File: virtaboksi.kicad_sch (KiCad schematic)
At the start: 22 parts, among them J1 Conn_01x02_Female, J2 Conn_01x03_Female, J3 Conn_01x02_Female, J4 Conn_01x02_Female, J5 Conn_01x02_Female, J6 Conn_01x02_Female, J7 Conn_01x02_Female, Q1 IRF9540N, Q2 IRF9540N, Q3 IRF9540N

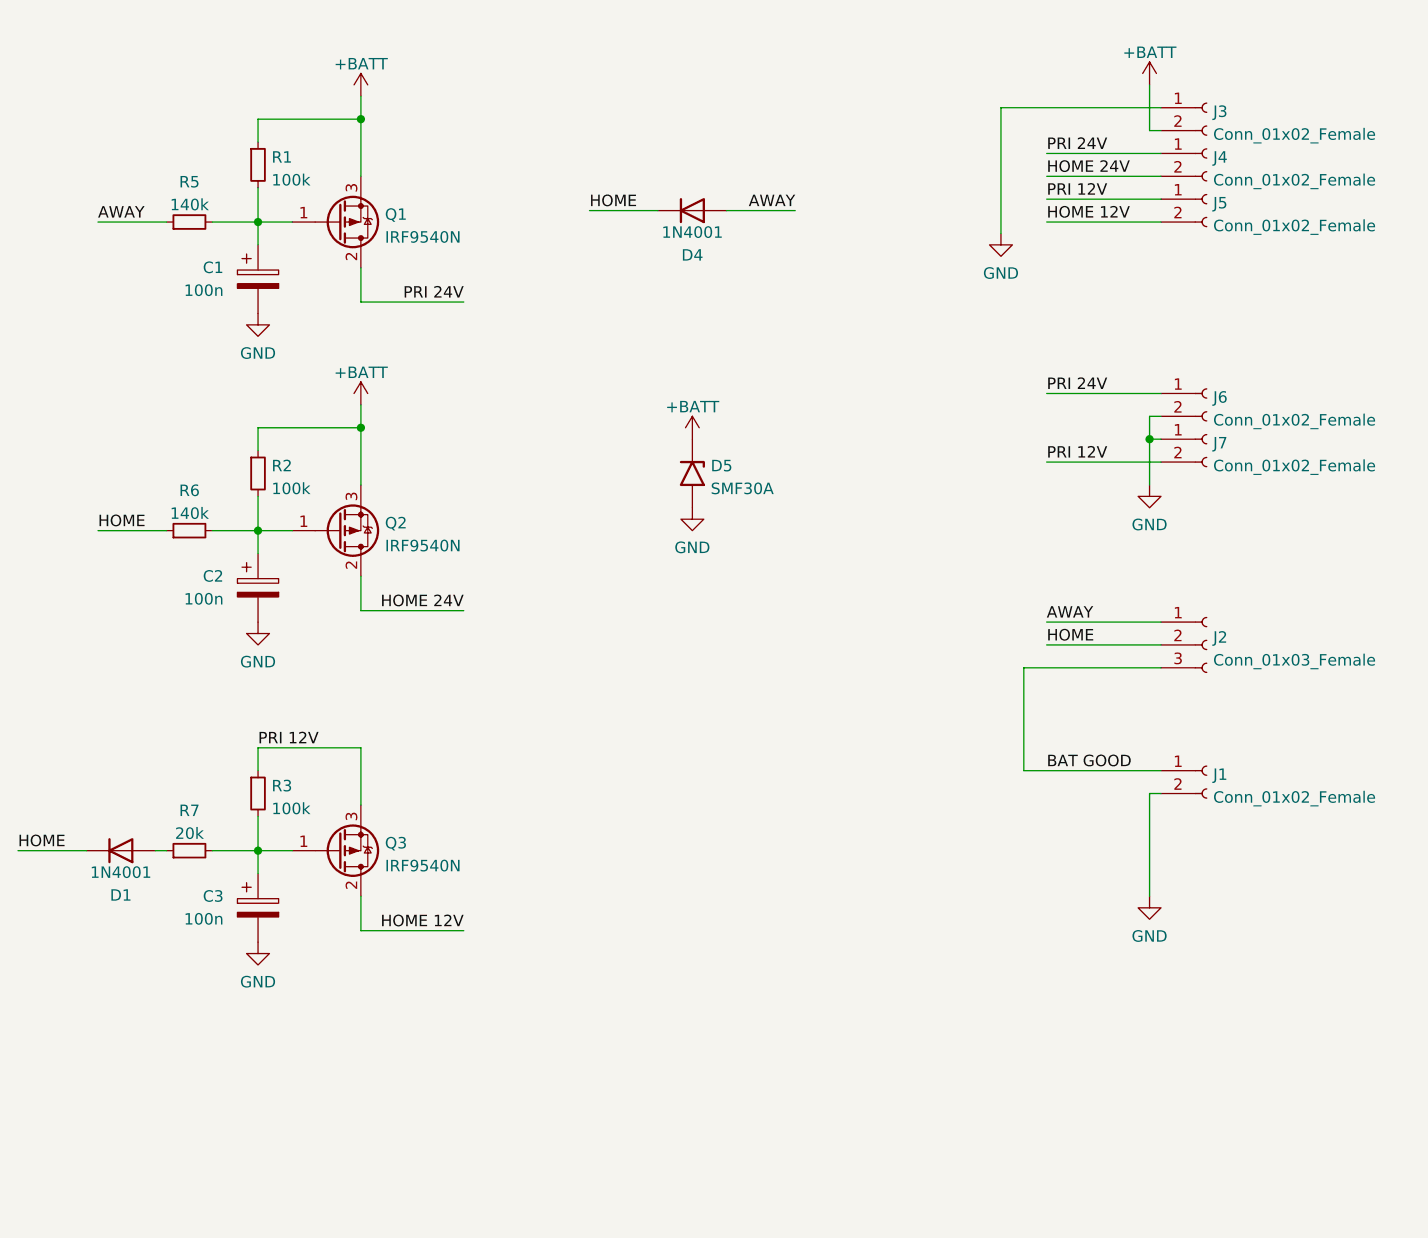
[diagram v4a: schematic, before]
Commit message: Change caps from elco to ceramic, reannotate
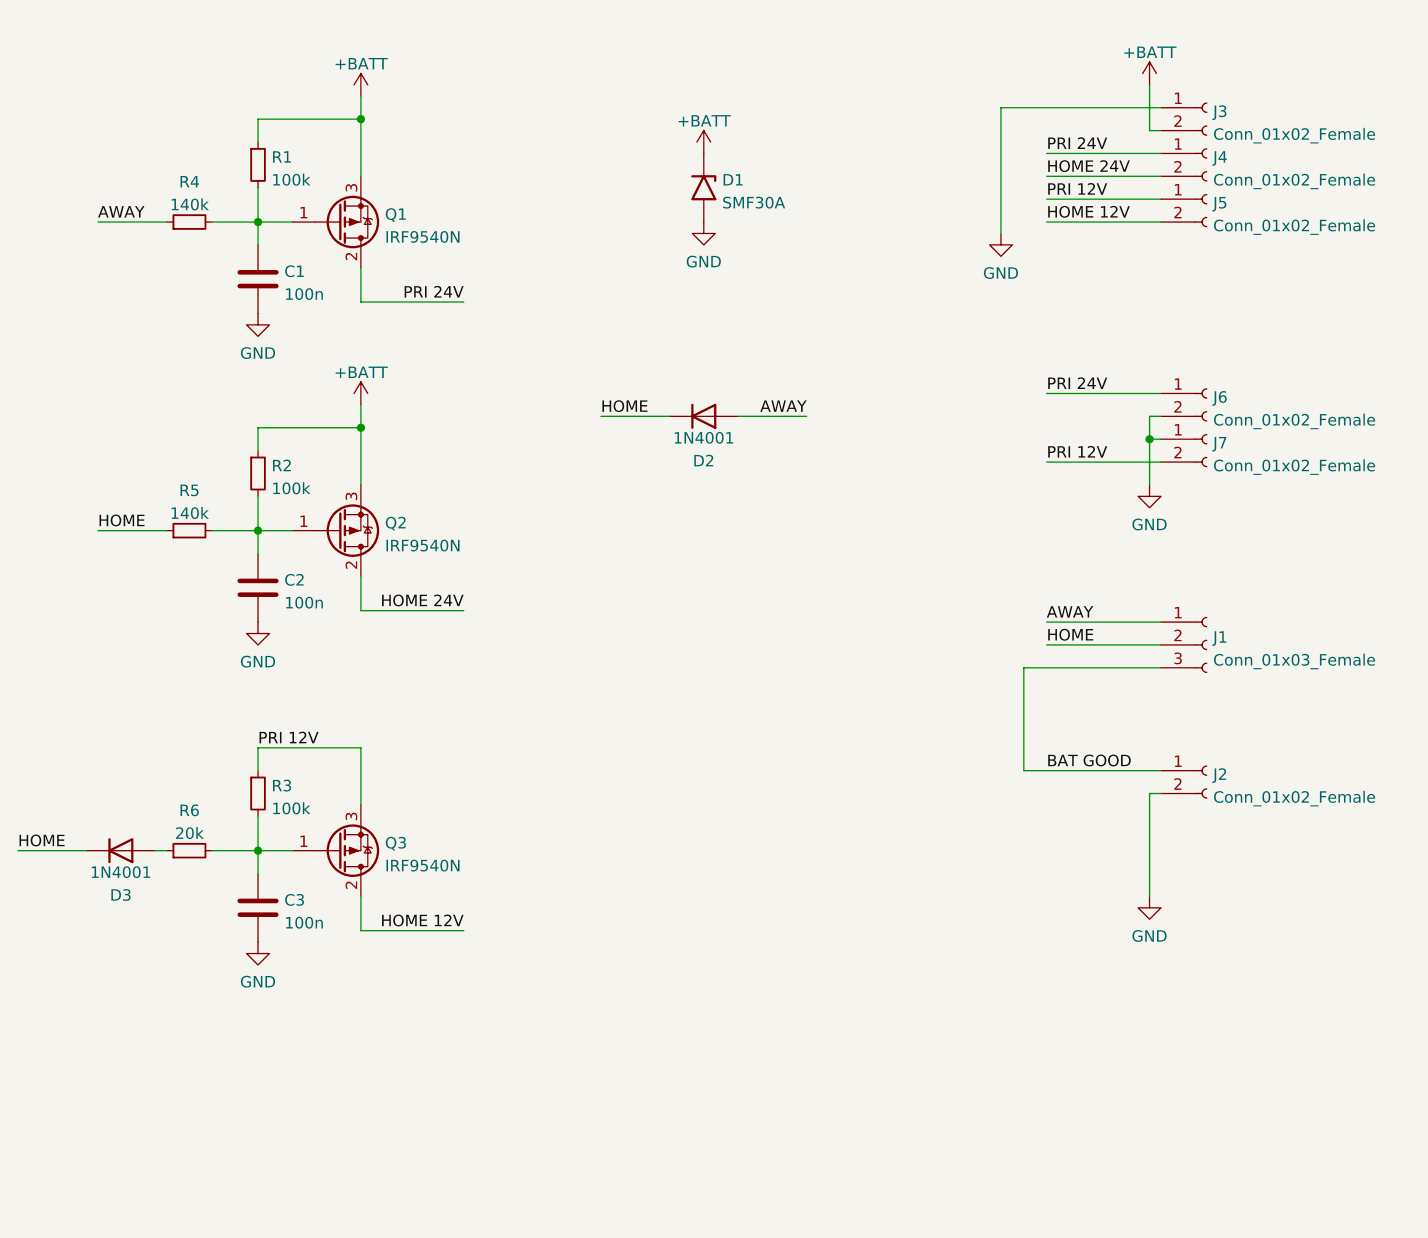
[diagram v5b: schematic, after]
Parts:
- removed C1, C2, C3: 100n, Capacitor_THT:CP_Radial_D6.3mm_P2.50mm, symbol Device:C_Polarized
- added C1, C2, C3: 100n, Capacitor_THT:C_Disc_D4.7mm_W2.5mm_P5.00mm, symbol Device:C
- renumbered D5 to D1, D4 to D2, D1 to D3, J2 to J1, J1 to J2, R5 to R4, R6 to R5, R7 to R6
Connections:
- net GND: now also C1.2, C2.2, C3.2
- net at Q1.1 (G), R1.2, R4.2: now also C1.1
- net at Q2.1 (G), R2.2, R5.2: now also C2.1
- net at Q3.1 (G), R3.2, R6.2: now also C3.1
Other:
- moved on the sheet: D1, D2

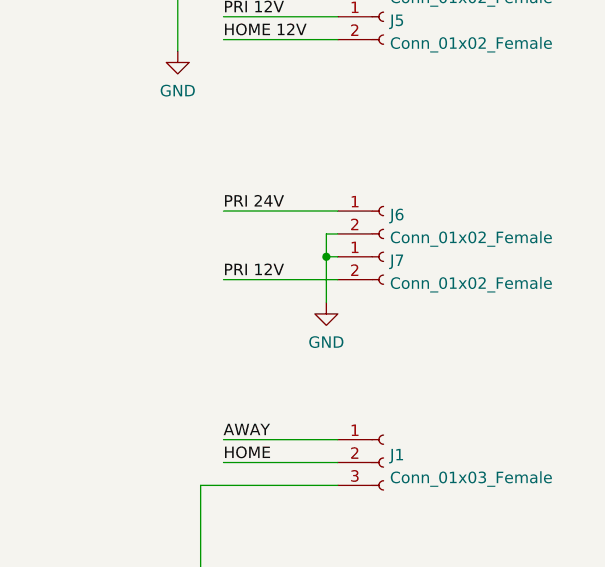
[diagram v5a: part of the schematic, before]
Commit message: Remove grounding pins for DC converter
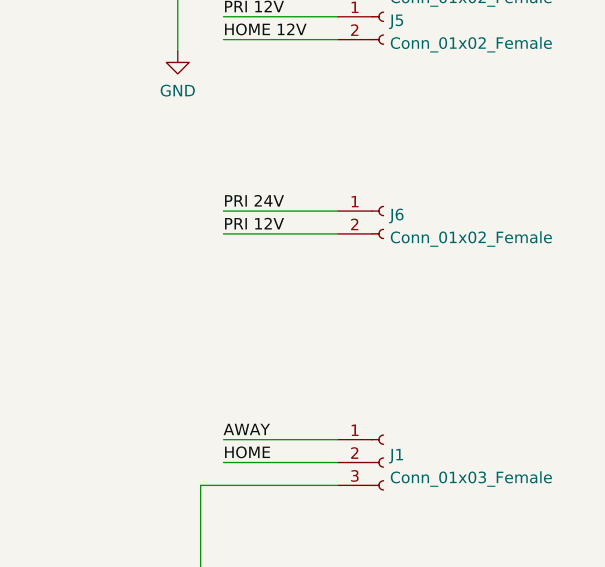
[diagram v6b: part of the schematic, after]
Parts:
- removed J7: Conn_01x02_Female, Powerpole:45A-VERT-PAIR, symbol Connector:Conn_01x02_Female
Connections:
- net GND: no longer J6.2 (Pin_2)
- net PRI 12V: now also J6.2 (Pin_2)
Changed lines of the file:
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@@
   (junction (at 76.2 72.39) (diameter 0) (color 0 0 0 0)
   )
-  (junction (at 163.83 73.66) (diameter 0) (color 0 0 0 0)
-  )
   (junction (at 76.2 38.1) (diameter 0) (color 0 0 0 0)
   )
@@
     (stroke (width 0) (type default) (color 0 0 0 0))
   )
-  (wire (pts (xy 163.83 73.66) (xy 165.1 73.66))
-    (stroke (width 0) (type default) (color 0 0 0 0))
-  )
   (wire (pts (xy 152.4 93.98) (xy 165.1 93.98))
     (stroke (width 0) (type default) (color 0 0 0 0))
@@
     (stroke (width 0) (type default) (color 0 0 0 0))
   )
-  (wire (pts (xy 163.83 71.12) (xy 163.83 73.66))
-    (stroke (width 0) (type default) (color 0 0 0 0))
-  )
   (wire (pts (xy 152.4 68.58) (xy 165.1 68.58))
     (stroke (width 0) (type default) (color 0 0 0 0))
@@
     (stroke (width 0) (type default) (color 0 0 0 0))
   )
-  (wire (pts (xy 163.83 71.12) (xy 165.1 71.12))
-    (stroke (width 0) (type default) (color 0 0 0 0))
-  )
   (wire (pts (xy 147.32 36.83) (xy 147.32 50.8))
     (stroke (width 0) (type default) (color 0 0 0 0))
@@
     (stroke (width 0) (type default) (color 0 0 0 0))
   )
-  (wire (pts (xy 152.4 76.2) (xy 165.1 76.2))
+  (wire (pts (xy 152.4 71.12) (xy 165.1 71.12))
     (stroke (width 0) (type default) (color 0 0 0 0))
   )
@@
   )
   (wire (pts (xy 87.63 92.71) (xy 76.2 92.71))
-    (stroke (width 0) (type default) (color 0 0 0 0))
-  )
-  (wire (pts (xy 163.83 73.66) (xy 163.83 78.74))
     (stroke (width 0) (type default) (color 0 0 0 0))
   )
@@
     (effects (font (size 1.27 1.27)) (justify right bottom))
   )
-  (label "PRI 12V" (at 152.4 76.2 0)
+  (label "PRI 12V" (at 152.4 71.12 0)
     (effects (font (size 1.27 1.27)) (justify left bottom))
   )
@@
     )
     (property "Datasheet" "" (id 3) (at 76.2 69.85 0)
-      (effects (font (size 1.27 1.27)) hide)
-    )
-    (pin "1")
-  )
-  (symbol (lib_id "power:GND") (at 163.83 78.74 0) (unit 1)
-    (in_bom yes) (on_board yes) (fields_autoplaced)
-    (property "Reference" "#PWR03" (id 0) (at 163.83 85.09 0)
-      (effects (font (size 1.27 1.27)) hide)
-    )
-    (property "Value" "GND" (id 1) (at 163.83 83.1834 0))
-    (property "Footprint" "" (id 2) (at 163.83 78.74 0)
-      (effects (font (size 1.27 1.27)) hide)
-    )
-    (property "Datasheet" "" (id 3) (at 163.83 78.74 0)
       (effects (font (size 1.27 1.27)) hide)
     )
@@
     (pin "2")
   )
-  (symbol (lib_id "Connector:Conn_01x02_Female") (at 170.18 73.66 0) (unit 1)
-    (in_bom yes) (on_board yes) (fields_autoplaced)
-    (property "Reference" "J7" (id 0) (at 170.8912 74.0953 0)
-      (effects (font (size 1.27 1.27)) (justify left))
-    )
-    (property "Value" "Conn_01x02_Female" (id 1) (at 170.8912 76.6322 0)
-      (effects (font (size 1.27 1.27)) (justify left))
-    )
-    (property "Footprint" "Powerpole:45A-VERT-PAIR" (id 2) (at 170.18 73.66 0)
-      (effects (font (size 1.27 1.27)) hide)
-    )
-    (property "Datasheet" "~" (id 3) (at 170.18 73.66 0)
-      (effects (font (size 1.27 1.27)) hide)
-    )
-    (pin "1")
-    (pin "2")
-  )
   (symbol (lib_id "Connector:Conn_01x02_Female") (at 170.18 68.58 0) (unit 1)
     (in_bom yes) (on_board yes) (fields_autoplaced)
@@
       (reference "#PWR02") (unit 1) (value "GND") (footprint "")
     )
-    (path "/42891e2c-f800-429f-9906-80cd4725b731"
-      (reference "#PWR03") (unit 1) (value "GND") (footprint "")
-    )
     (path "/eaa8ab04-f6f6-460a-a2bc-4d05ae63606d"
       (reference "#PWR04") (unit 1) (value "+BATT") (footprint "")
@@
       (reference "J6") (unit 1) (value "Conn_01x02_Female") (footprint "Powerpole:45A-VERT-PAIR")
     )
-    (path "/babf2911-162e-47f9-9992-86deeace1a71"
-      (reference "J7") (unit 1) (value "Conn_01x02_Female") (footprint "Powerpole:45A-VERT-PAIR")
-    )
     (path "/6544545a-25b2-4ef2-865d-726b8315cab6"

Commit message: Add image
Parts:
- Q1, Q2, Q3: value IRF9540N -> IRF4905; symbol Transistor_FET:IRF9540N -> Transistor_FET:IRF4905
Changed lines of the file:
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@@
     (pin "3")
   )
-  (symbol (lib_id "Transistor_FET:IRF9540N") (at 73.66 49.53 0) (mirror x) (unit 1)
-    (in_bom yes) (on_board yes) (fields_autoplaced)
-    (property "Reference" "Q1" (id 0) (at 78.867 48.6953 0)
-      (effects (font (size 1.27 1.27)) (justify left))
-    )
-    (property "Value" "IRF9540N" (id 1) (at 78.867 51.2322 0)
+  (symbol (lib_id "Transistor_FET:IRF4905") (at 73.66 49.53 0) (mirror x) (unit 1)
+    (in_bom yes) (on_board yes)
+    (property "Reference" "Q1" (id 0) (at 78.74 48.26 0)
+      (effects (font (size 1.27 1.27)) (justify left))
+    )
+    (property "Value" "IRF4905" (id 1) (at 78.74 50.8 0)
       (effects (font (size 1.27 1.27)) (justify left))
     )
@@
       (effects (font (size 1.27 1.27) italic) (justify left) hide)
     )
-    (property "Datasheet" "http://www.irf.com/product-info/datasheets/data/irf9540n.pdf" (id 3) (at 73.66 49.53 0)
+    (property "Datasheet" "http://www.infineon.com/dgdl/irf4905.pdf?fileId=5546d462533600a4015355e32165197c" (id 3) (at 73.66 49.53 0)
       (effects (font (size 1.27 1.27)) (justify left) hide)
     )
@@
     (pin "2")
   )
-  (symbol (lib_id "Transistor_FET:IRF9540N") (at 73.66 83.82 0) (mirror x) (unit 1)
-    (in_bom yes) (on_board yes) (fields_autoplaced)
-    (property "Reference" "Q2" (id 0) (at 78.867 82.9853 0)
-      (effects (font (size 1.27 1.27)) (justify left))
-    )
-    (property "Value" "IRF9540N" (id 1) (at 78.867 85.5222 0)
+  (symbol (lib_id "Transistor_FET:IRF4905") (at 73.66 83.82 0) (mirror x) (unit 1)
+    (in_bom yes) (on_board yes)
+    (property "Reference" "Q2" (id 0) (at 78.74 82.55 0)
+      (effects (font (size 1.27 1.27)) (justify left))
+    )
+    (property "Value" "IRF4905" (id 1) (at 78.74 85.09 0)
       (effects (font (size 1.27 1.27)) (justify left))
     )
@@
       (effects (font (size 1.27 1.27) italic) (justify left) hide)
     )
-    (property "Datasheet" "http://www.irf.com/product-info/datasheets/data/irf9540n.pdf" (id 3) (at 73.66 83.82 0)
+    (property "Datasheet" "http://www.infineon.com/dgdl/irf4905.pdf?fileId=5546d462533600a4015355e32165197c" (id 3) (at 73.66 83.82 0)
       (effects (font (size 1.27 1.27)) (justify left) hide)
     )
@@
     (pin "2")
   )
-  (symbol (lib_id "Transistor_FET:IRF9540N") (at 73.66 119.38 0) (mirror x) (unit 1)
-    (in_bom yes) (on_board yes) (fields_autoplaced)
-    (property "Reference" "Q3" (id 0) (at 78.867 118.5453 0)
-      (effects (font (size 1.27 1.27)) (justify left))
-    )
-    (property "Value" "IRF9540N" (id 1) (at 78.867 121.0822 0)
+  (symbol (lib_id "Transistor_FET:IRF4905") (at 73.66 119.38 0) (mirror x) (unit 1)
+    (in_bom yes) (on_board yes)
+    (property "Reference" "Q3" (id 0) (at 78.74 118.11 0)
+      (effects (font (size 1.27 1.27)) (justify left))
+    )
+    (property "Value" "IRF4905" (id 1) (at 78.74 120.65 0)
       (effects (font (size 1.27 1.27)) (justify left))
     )
@@
       (effects (font (size 1.27 1.27) italic) (justify left) hide)
     )
-    (property "Datasheet" "http://www.irf.com/product-info/datasheets/data/irf9540n.pdf" (id 3) (at 73.66 119.38 0)
+    (property "Datasheet" "http://www.infineon.com/dgdl/irf4905.pdf?fileId=5546d462533600a4015355e32165197c" (id 3) (at 73.66 119.38 0)
       (effects (font (size 1.27 1.27)) (justify left) hide)
     )
@@
     )
     (path "/6544545a-25b2-4ef2-865d-726b8315cab6"
-      (reference "Q1") (unit 1) (value "IRF9540N") (footprint "Package_TO_SOT_THT:TO-220-3_Vertical")
+      (reference "Q1") (unit 1) (value "IRF4905") (footprint "Package_TO_SOT_THT:TO-220-3_Vertical")
     )
     (path "/7b533f0b-6d32-4073-9d6a-f269e92ed0c6"
-      (reference "Q2") (unit 1) (value "IRF9540N") (footprint "Package_TO_SOT_THT:TO-220-3_Vertical")
+      (reference "Q2") (unit 1) (value "IRF4905") (footprint "Package_TO_SOT_THT:TO-220-3_Vertical")
     )
     (path "/c09b0fec-a6f6-4bd9-ac43-97014c428ec5"
-      (reference "Q3") (unit 1) (value "IRF9540N") (footprint "Package_TO_SOT_THT:TO-220-3_Vertical")
+      (reference "Q3") (unit 1) (value "IRF4905") (footprint "Package_TO_SOT_THT:TO-220-3_Vertical")
     )
     (path "/53237060-a0bd-4bf0-8bbe-9c98dba89747"
